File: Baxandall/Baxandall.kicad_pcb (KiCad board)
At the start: 4 copper layers, 32 x 60 mm, 25 parts, among them J1 Conn_02x04_Odd_Even, J2 Conn_02x04_Odd_Even, U1 OPA1656, U2 BUF634AxD

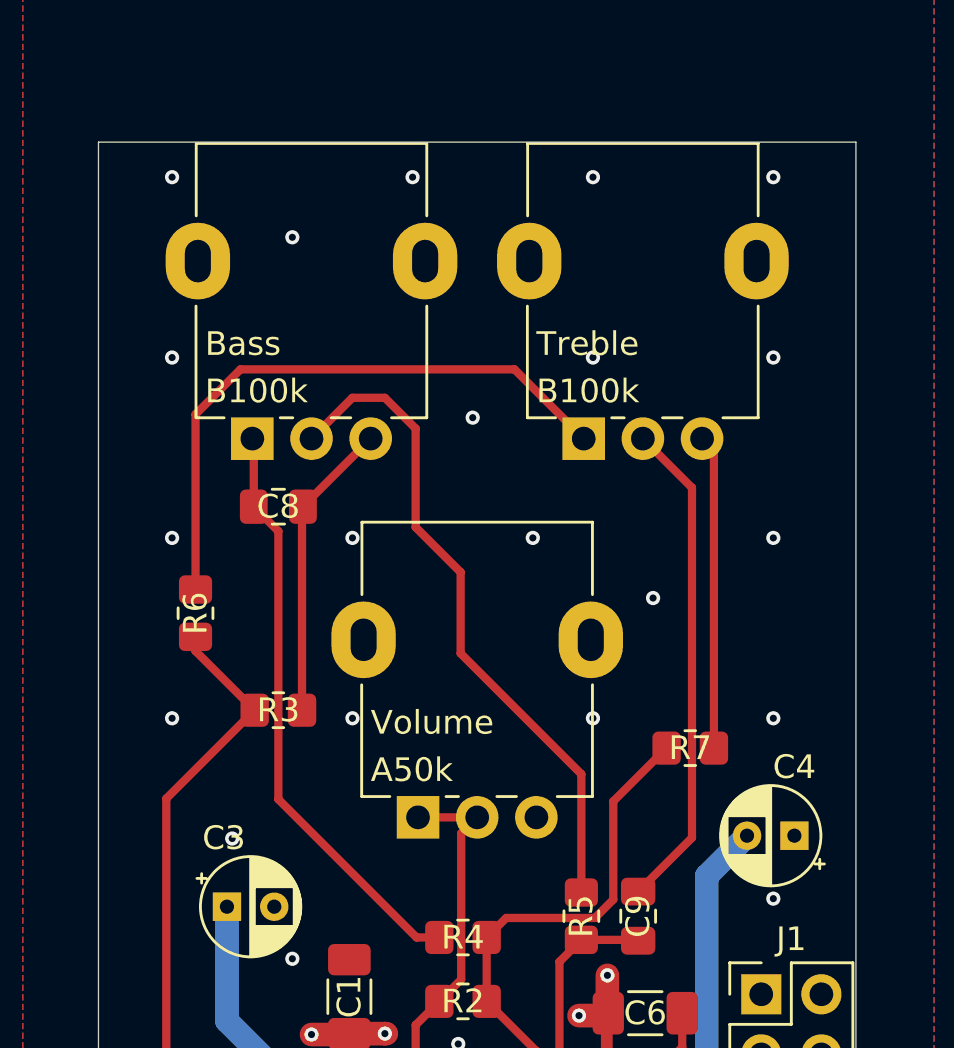
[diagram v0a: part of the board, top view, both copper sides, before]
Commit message: Add tentative drill patterns for Tayda enclosure drilling
Fix up the layout so that the same drill pattern with three holes for
pots/switches works for both the Baxandall and Boost, and move some of
the other controls around to make for whole numbers in mm.

Do the drill patterns work? They match the PCB layout, but let's see
about the vertical sides...  Tayda drilling is running behind, so I
don't think I'll see the actual result for a couple of weeks.

Also fix some typos in the readme while updating it about the drill
patterns.

Signed-off-by: Linus Torvalds <torvalds@linux-foundation.org>
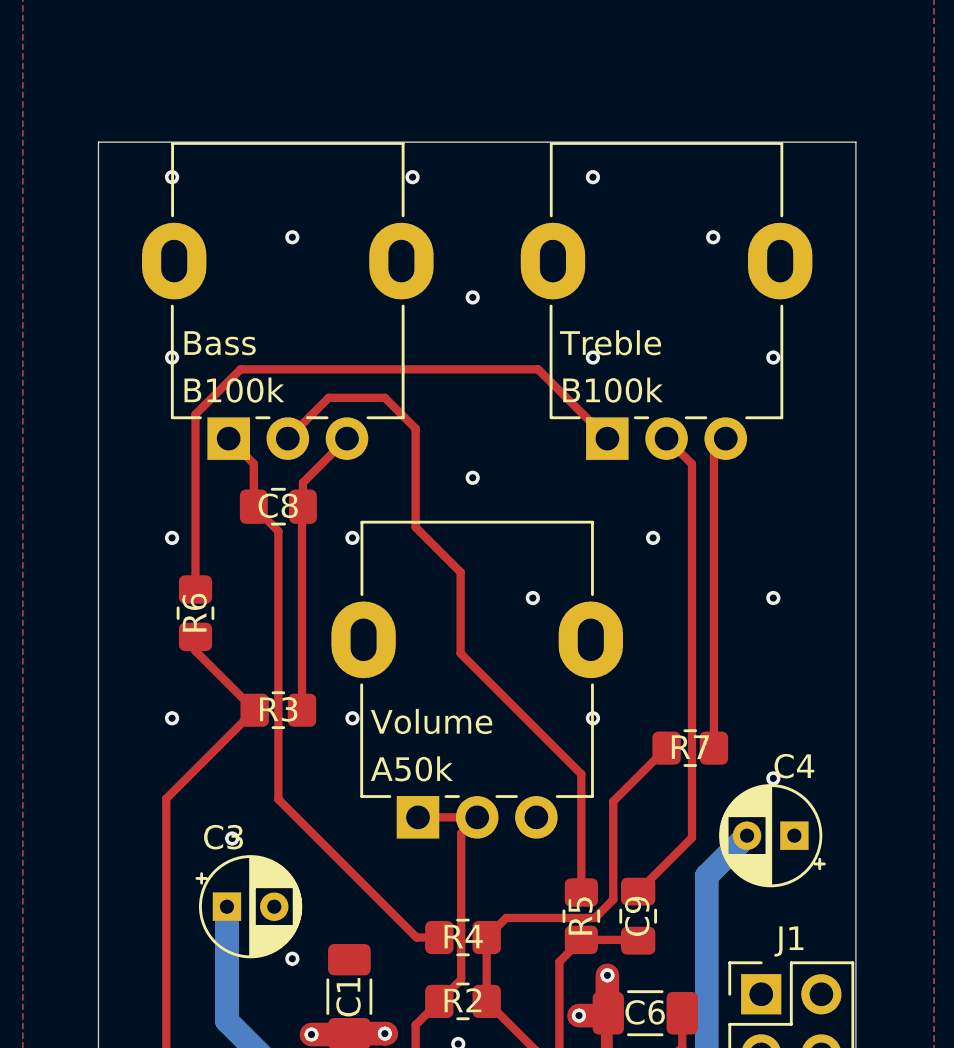
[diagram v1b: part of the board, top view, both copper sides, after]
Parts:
- moved RV2 1.00 mm to (89.5, 75.5)
- moved RV3 1.00 mm to (105.5, 75.5)
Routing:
- net Net-(R6-Pad1): track 25.8 -> 26.8 mm
- net Net-(R5-Pad1): track 28.2 -> 29.2 mm
- net Net-(R7-Pad2): track 12.6 -> 13.3 mm
- net Net-(C8-Pad2): track 24.8 -> 25.3 mm
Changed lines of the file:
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@@
 	(footprint "Potentiometer_THT:Potentiometer_Alpha_RD901F-40-00D_Single_Vertical"
 		(layer "F.Cu")
-		(at 104.5 75.525 90)
+		(at 105.5 75.525 90)
 		(descr "Potentiometer, vertical, 9mm, single, http://www.taiwanalpha.com.tw/downloads?target=products&id=113")
 		(tags "potentiometer vertical 9mm single")
@@
 	(footprint "Potentiometer_THT:Potentiometer_Alpha_RD901F-40-00D_Single_Vertical"
 		(layer "F.Cu")
-		(at 90.5 75.525 90)
+		(at 89.5 75.525 90)
 		(descr "Potentiometer, vertical, 9mm, single, http://www.taiwanalpha.com.tw/downloads?target=products&id=113")
 		(tags "potentiometer vertical 9mm single")
@@
 	)
 	(via
-		(at 94.73 79.7195)
+		(at 87.11 87.3395)
 		(size 0.6)
 		(drill 0.3)
@@
 	)
 	(via
-		(at 112.51 79.7195)
+		(at 107.43 79.7195)
 		(size 0.6)
 		(drill 0.3)
@@
 	)
 	(via
-		(at 99.81 74.6395)
+		(at 104.89 87.3395)
 		(size 0.6)
 		(drill 0.3)
@@
 	)
 	(via
-		(at 102.35 110.1995)
+		(at 104.89 64.4795)
 		(size 0.6)
 		(drill 0.3)
@@
 	)
 	(via
-		(at 87.11 87.3395)
+		(at 94.73 87.3395)
 		(size 0.6)
 		(drill 0.3)
@@
 	)
 	(via
-		(at 107.43 82.2595)
+		(at 109.97 67.0195)
 		(size 0.6)
 		(drill 0.3)
@@
 	)
 	(via
-		(at 112.51 110.1995)
+		(at 107.43 112.7395)
 		(size 0.6)
 		(drill 0.3)
@@
 	)
 	(via
-		(at 94.73 87.3395)
+		(at 87.11 64.4795)
 		(size 0.6)
 		(drill 0.3)
@@
 	)
 	(via
-		(at 112.51 72.0995)
+		(at 92.19 67.0195)
 		(size 0.6)
 		(drill 0.3)
@@
 	)
 	(via
-		(at 99.81 115.2795)
+		(at 104.89 72.0995)
 		(size 0.6)
 		(drill 0.3)
@@
 	)
 	(via
-		(at 97.27 64.4795)
+		(at 102.35 82.2595)
 		(size 0.6)
 		(drill 0.3)
@@
 	)
 	(via
-		(at 112.51 64.4795)
+		(at 87.11 79.7195)
 		(size 0.6)
 		(drill 0.3)
@@
 	)
 	(via
-		(at 112.51 87.3395)
+		(at 99.81 115.2795)
 		(size 0.6)
 		(drill 0.3)
@@
 	)
 	(via
-		(at 107.43 105.1195)
+		(at 94.73 79.7195)
 		(size 0.6)
 		(drill 0.3)
@@
 	)
 	(via
-		(at 104.89 87.3395)
+		(at 109.97 117.8195)
 		(size 0.6)
 		(drill 0.3)
@@
 	)
 	(via
-		(at 92.19 67.0195)
+		(at 102.35 120.3595)
 		(size 0.6)
 		(drill 0.3)
@@
 	)
 	(via
-		(at 87.11 64.4795)
+		(at 97.27 64.4795)
 		(size 0.6)
 		(drill 0.3)
@@
 	)
 	(via
-		(at 107.43 112.7395)
+		(at 112.51 89.8795)
 		(size 0.6)
 		(drill 0.3)
@@
 	)
 	(via
-		(at 87.11 79.7195)
+		(at 99.81 69.5595)
 		(size 0.6)
 		(drill 0.3)
@@
 	)
 	(via
-		(at 89.65 92.4195)
+		(at 112.51 110.1995)
 		(size 0.6)
 		(drill 0.3)
@@
 	)
 	(via
-		(at 92.19 120.3595)
+		(at 92.19 97.4995)
 		(size 0.6)
 		(drill 0.3)
@@
 	)
 	(via
-		(at 104.89 64.4795)
+		(at 94.73 112.7395)
 		(size 0.6)
 		(drill 0.3)
@@
 	)
 	(via
-		(at 109.97 117.8195)
+		(at 102.35 110.1995)
 		(size 0.6)
 		(drill 0.3)
@@
 	)
 	(via
-		(at 92.19 97.4995)
+		(at 112.51 72.0995)
 		(size 0.6)
 		(drill 0.3)
@@
 	)
 	(via
-		(at 99.2 101.1)
+		(at 107.43 105.1195)
 		(size 0.6)
 		(drill 0.3)
@@
 	)
 	(via
-		(at 102.35 79.7195)
+		(at 99.81 77.1795)
 		(size 0.6)
 		(drill 0.3)
@@
 	)
 	(via
-		(at 112.51 94.9595)
+		(at 92.19 120.3595)
 		(size 0.6)
 		(drill 0.3)
@@
 	)
 	(via
-		(at 104.89 72.0995)
+		(at 99.2 101.1)
 		(size 0.6)
 		(drill 0.3)
@@
 	)
 	(via
-		(at 102.35 120.3595)
+		(at 112.51 82.2595)
 		(size 0.6)
 		(drill 0.3)
@@
 	)
 	(via
-		(at 94.73 112.7395)
+		(at 89.65 92.4195)
 		(size 0.6)
 		(drill 0.3)
@@
 	(segment
 		(start 90.5625 78.4)
-		(end 90.5625 75.5875)
+		(end 90.5625 76.5875)
 		(width 0.35)
 		(layer "F.Cu")
@@
 	)
 	(segment
+		(start 90.5625 76.5875)
+		(end 89.5 75.525)
+		(width 0.35)
+		(layer "F.Cu")
+		(net 3)
+	)
+	(segment
+		(start 92.6375 78.4)
+		(end 92.6375 77.3875)
+		(width 0.35)
+		(layer "F.Cu")
+		(net 4)
+	)
+	(segment
 		(start 92.6 87)
 		(end 92.6 78.4375)
@@
 	)
 	(segment
-		(start 92.6375 78.3875)
-		(end 95.5 75.525)
+		(start 92.6375 77.3875)
+		(end 94.5 75.525)
 		(width 0.35)
 		(layer "F.Cu")
@@
 	)
 	(segment
-		(start 109.075 77.6)
-		(end 107 75.525)
+		(start 109.075 76.6)
+		(end 108 75.525)
 		(width 0.35)
 		(layer "F.Cu")
@@
 	(segment
 		(start 109.075 92.3875)
-		(end 109.075 77.6)
+		(end 109.075 76.6)
 		(width 0.35)
 		(layer "F.Cu")
@@
 	)
 	(segment
-		(start 99.3 81.16795)
-		(end 97.4 79.26795)
+		(start 96.1 73.8)
+		(end 93.725 73.8)
 		(width 0.35)
 		(layer "F.Cu")
@@
 	)
 	(segment
-		(start 104.4 89.7)
-		(end 99.3 84.6)
+		(start 97.4 75.1)
+		(end 96.1 73.8)
 		(width 0.35)
 		(layer "F.Cu")
@@
 	)
 	(segment
-		(start 99.3 84.6)
-		(end 99.3 81.16795)
+		(start 97.4 79.26795)
+		(end 97.4 75.1)
 		(width 0.35)
 		(layer "F.Cu")
@@
 	)
 	(segment
-		(start 104.4 94.7)
-		(end 104.4 89.7)
+		(start 104.4 89.7)
+		(end 99.3 84.6)
 		(width 0.35)
 		(layer "F.Cu")
@@
 	)
 	(segment
-		(start 94.725 73.8)
-		(end 93 75.525)
+		(start 99.3 84.6)
+		(end 99.3 81.16795)
 		(width 0.35)
 		(layer "F.Cu")
@@
 	)
 	(segment
-		(start 96.1 73.8)
-		(end 94.725 73.8)
+		(start 99.3 81.16795)
+		(end 97.4 79.26795)
 		(width 0.35)
 		(layer "F.Cu")
@@
 	)
 	(segment
-		(start 97.4 75.1)
-		(end 96.1 73.8)
+		(start 93.725 73.8)
+		(end 92 75.525)
 		(width 0.35)
 		(layer "F.Cu")
@@
 	)
 	(segment
-		(start 97.4 79.26795)
-		(end 97.4 75.1)
+		(start 104.4 94.7)
+		(end 104.4 89.7)
 		(width 0.35)
 		(layer "F.Cu")
@@
 	)
 	(segment
-		(start 101.575 72.6)
-		(end 104.5 75.525)
+		(start 88.1 74.5)
+		(end 90 72.6)
 		(width 0.35)
 		(layer "F.Cu")
@@
 	)
 	(segment
-		(start 88.1 74.5)
-		(end 90 72.6)
+		(start 102.575 72.6)
+		(end 105.5 75.525)
 		(width 0.35)
 		(layer "F.Cu")
@@
 	(segment
 		(start 90 72.6)
-		(end 101.575 72.6)
+		(end 102.575 72.6)
 		(width 0.35)
 		(layer "F.Cu")
@@
 	)
 	(segment
+		(start 110 76.025)
+		(end 110.5 75.525)
+		(width 0.35)
+		(layer "F.Cu")
+		(net 15)
+	)
+	(segment
 		(start 86.865 114.365)
 		(end 86.865 90.735)
@@
 	)
 	(group "ViaStitching GND"
-		(members "094a4eb0-3243-4cbd-99c0-290de56c2e0b" "0f3cf215-10fd-4587-87e2-e741cb64b007"
-			"10b88feb-e1da-49c3-881f-73d7e2af6bf1" "15e68d17-3ded-4d61-b84c-fc83e2cf205b"
-			"1887e62c-1e44-49a0-9621-163199de8e7c" "23591f09-9029-4015-b4e7-08c6aeffa8c1"
-			"3ec8e87f-1912-49cd-929d-cf347ee1b7b7" "3f3d5dfb-3587-440f-a77d-b81e37bce360"
-			"615552bd-fea0-4226-9853-83c1f36515c4" "66de3156-b7c4-4d48-98fb-a944bf77b1c4"
-			"68b8b6b0-c93c-4e01-9556-b64525026885" "75e10863-0c61-4797-9c86-305966023d28"
-			"832ea664-f17a-4a34-80a2-9170f4736ae3" "88439968-cea6-44dd-9059-cbaa9344042d"
-			"91cbf0ef-6bd9-4652-b537-cfd49262f781" "965658d3-35e8-4113-b3e0-a8360ffb0ee8"
-			"9f877f0b-db0b-4985-bebc-aecce1885755" "a7f67d84-ff33-4f63-b252-2f9d87f189e0"
-			"b68ec87c-cd6b-4b65-9f3b-c7956056f70e" "bc46adc7-ffbe-4fb9-a742-0ef2d4ba0f6d"
-			"c61f8958-ae5d-4f4f-a0da-499590e687f0" "c7ff196e-5e6b-42c9-a01d-f83fea95d68a"
-			"c8aaaccb-83c6-40f6-8c5c-6842b389eefb" "e2596cc1-707c-47b7-b739-c25ca806c4f1"
-			"e811741d-3f1e-4f8c-8f4a-c02ad152c1f1" "f39771c9-1004-42fd-ab80-10c43e673a3f"
-			"f630a7cb-f53a-424b-b84f-7f2a457e7246" "f7a1bfc0-c328-4223-9af7-6ac82cbc8324"
-			"fa457983-3180-4349-a0c2-9dff6d0ce808" "fbb238a3-e490-444c-94b2-f851ce9665e3"
+		(members "139fbca9-dc89-48e1-8c32-6039b5031c6d" "1ec47df8-8d81-4532-b319-682781823970"
+			"2a088947-757e-40b3-b9cd-464c6795013c" "32c83054-514d-4d05-bdd0-ca1ba4d84823"
+			"3c3272ee-4d0a-4f80-9a91-2115786afad6" "3f7b804e-2cba-4d7a-ac82-2d950e75f7f7"
+			"515e3c0a-75e4-4a78-8a65-285fdb93fcfc" "551122cb-603f-456f-94bd-ce3a9a4396d3"
+			"56fe9160-e2ae-4581-9741-c63422a0d49b" "5c33ef87-117c-4329-942a-8c725042443b"
+			"5f91aa5a-29f4-4d4c-b51e-f69cccaf5604" "640c8a33-f044-4e71-abeb-ec78863bbbf9"
+			"6fbb1a5c-ebca-4991-abb6-af30266196b5" "746e3383-67a0-429a-b78b-f03f1cbfd9c6"
+			"7685b137-ab52-4047-9fba-20e0a48b84e5" "8269fc93-b609-4087-81af-514fea4d62df"
+			"93ab523b-2e05-4cf4-b443-737de7c950b4" "95355b55-16f9-47a9-9b0e-004da6068eca"
+			"97f50c7a-538b-4274-9318-fff3dc56c6e9" "98ae6132-0a94-42c6-a838-4b93f1991fb3"
+			"9b4d58e6-35f2-4551-93a1-bd3564d9daa0" "a13ca90f-b954-4dd2-84ef-283094c0842d"
+			"af59ad03-1e79-4293-bbac-ce54e1297d0c" "c2db6aab-3e0e-4e29-8204-d2df4ef0b111"
+			"cc2f9f62-f95a-4831-8e28-e210d93cbab5" "cc8f2a1e-e7a1-40d8-9f07-ac6e37e3524a"
+			"e45752ef-70cb-4ede-b1bd-90f07e79434d" "ebf4deff-e394-42da-a50c-f37f4cc9aac0"
+			"f871870e-038b-4307-8b53-80591b5cc260" "f94c1044-9e31-4c56-8559-fce233c22bb4"
 		)
 	)
